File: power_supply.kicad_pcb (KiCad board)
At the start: 2 copper layers, 50 x 100 mm, 32 parts, among them P1 GND, P10 6.3_AC, P11 HEAT, P12 HEAT, P13 R+, P2 BIAS_AC, P3 BIAS_AC, P4 HT_AC, P5 HT_AC, P6 HT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

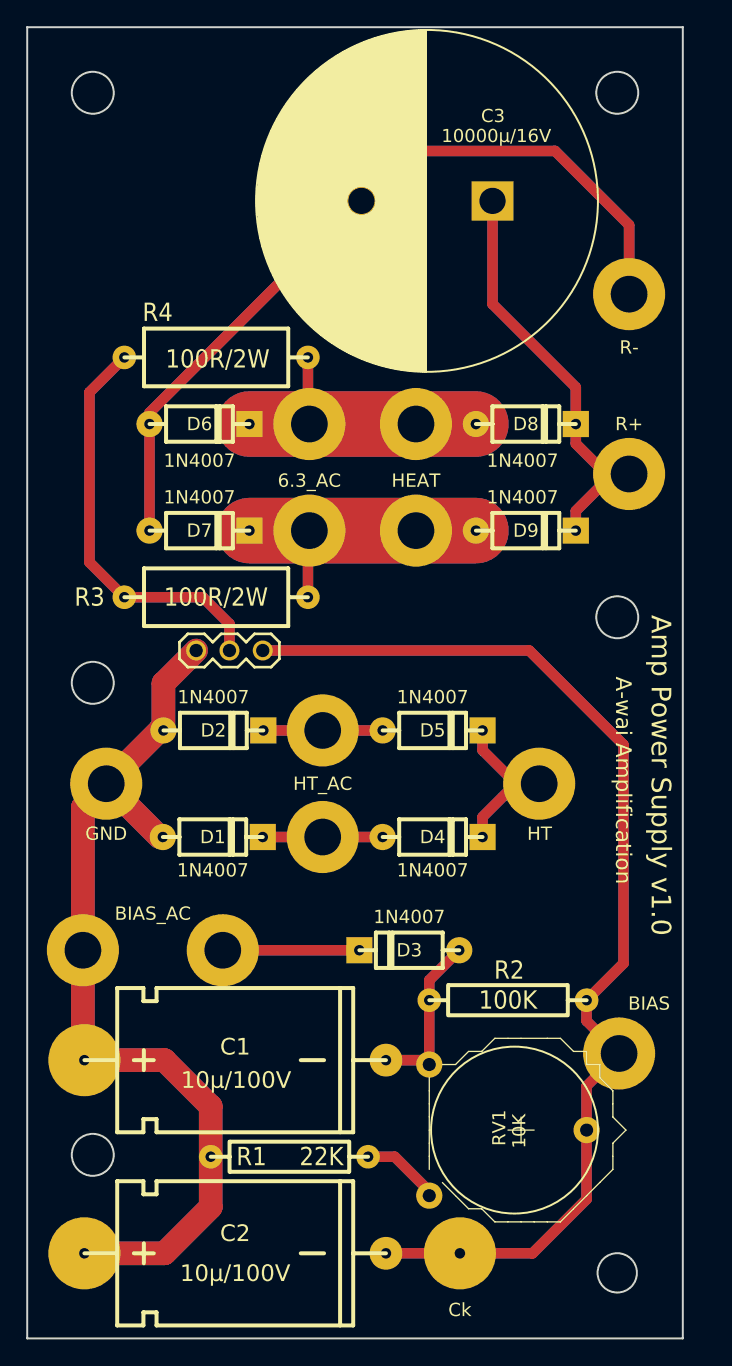
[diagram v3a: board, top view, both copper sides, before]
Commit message: Update for KiCAD v5
Signed-off-by: Arnaud Ferraris <arnaud.ferraris@gmail.com>
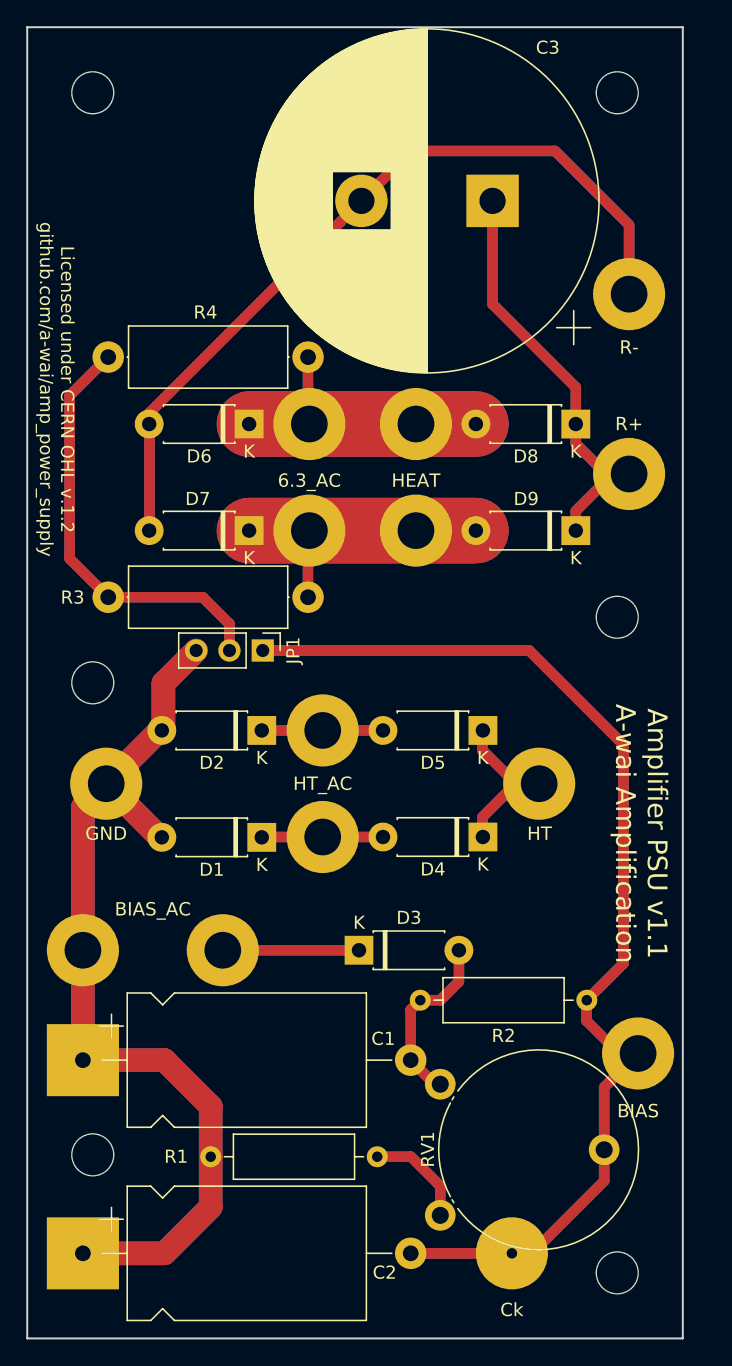
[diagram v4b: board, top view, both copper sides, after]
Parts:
- added REF**: MountingHole_3.2mm_M3, MountingHole:MountingHole_3.2mm_M3, F.Cu at (80.0, 136.0)
- added REF**: MountingHole_3.2mm_M3, MountingHole:MountingHole_3.2mm_M3, F.Cu at (120.0, 145.0)
- added REF**: MountingHole_3.2mm_M3, MountingHole:MountingHole_3.2mm_M3, F.Cu at (80.0, 55.0)
- added REF**: MountingHole_3.2mm_M3, MountingHole:MountingHole_3.2mm_M3, F.Cu at (120.0, 55.0)
- added REF**: MountingHole_3.2mm_M3, MountingHole:MountingHole_3.2mm_M3, F.Cu at (120.0, 95.0)
- added REF**: MountingHole_3.2mm_M3, MountingHole:MountingHole_3.2mm_M3, F.Cu at (80.0, 100.0)
- C1, C2: footprint ay_passive:CPA_10µF_160V -> Capacitor_THT:CP_Axial_L18.0mm_D10.0mm_P25.00mm_Horizontal
- C3: footprint Capacitors_ThroughHole:C_Radial_D26_L31_P10 -> Capacitor_THT:CP_Radial_D26.0mm_P10.00mm_SnapIn
- D1, D2, D3, D4, D5, D6, D7, D8, D9: footprint ay_passive:DIODE -> Diode_THT:D_DO-41_SOD81_P7.62mm_Horizontal
- JP1: footprint freetronics_footprints:1X03 -> Connector_PinHeader_2.54mm:PinHeader_1x03_P2.54mm_Vertical
- P1, P10, P11, P12, P13, P2, P3, P4, P5, P6, P7, P8, P9: footprint ay_turrets:TURRET -> ProjectLib:TURRET
- R1, R2: footprint ay_passive:R_0.5W -> Resistor_THT:R_Axial_DIN0309_L9.0mm_D3.2mm_P12.70mm_Horizontal
- R3, R4: footprint ay_passive:R_2W -> Resistor_THT:R_Axial_DIN0414_L11.9mm_D4.5mm_P15.24mm_Horizontal
- RV1: footprint Potentiometers:Potentiometer_Trimmer-Piher_PT15-V12-5_horizontal -> Potentiometer_THT:Potentiometer_Piher_PT-15-V02_Vertical
- moved C1 11.6 mm to (79.2, 128.8), turned to 0 degrees
- moved C2 11.6 mm to (79.2, 143.5), turned to 0 degrees
- moved RV1 11.5 mm to (106.5, 140.6), turned to 0 degrees
- moved R4 7.01 mm to (96.4, 75.2)
- moved R3 7.01 mm to (96.4, 93.5)
- moved R2 6.01 mm to (117.7, 124.2)
- moved R1 6.00 mm to (89.0, 136.1)
- moved T1 3.96 mm to (112.0, 143.5)
- moved D3 3.84 mm to (100.3, 120.4), turned to 0 degrees
- moved D4 3.84 mm to (109.8, 111.8), turned to 180 degrees
- moved D5 3.84 mm to (109.8, 103.6), turned to 180 degrees
- moved D8 3.81 mm to (116.8, 80.3), turned to 180 degrees
- moved D9 3.81 mm to (116.8, 88.4), turned to 180 degrees
- moved D6 3.78 mm to (91.9, 80.3), turned to 180 degrees
- moved D7 3.78 mm to (91.9, 88.4), turned to 180 degrees
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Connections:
- RV1 pad 1: Net-(C1-Pad2) -> Net-(R1-Pad2)
- RV1 pad 3: Net-(R1-Pad2) -> Net-(C1-Pad2)
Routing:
- net Net-(R1-Pad2): track 11.5 -> 15.9 mm
- net Net-(JP1-Pad2): track 62.8 -> 65.7 mm
- net /Vbias: track 170.7 -> 168.1 mm
- net Net-(C1-Pad2): track 25.3 -> 27.6 mm
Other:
- outline, holes or cut-outs redrawn
- board text added: "Amplifier PSU v1.1 A-wai Amplification"
- board text added: "Licensed under CERN OHL v.1.2 github.com/a-wai/amp_power_supply"
- board text removed: "A-wai Amplification"
- board text removed: "Amp Power Supply v1.0"
